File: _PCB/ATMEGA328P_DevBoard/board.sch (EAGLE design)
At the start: 35 parts, among them IC1 TP4056, IC2 DW01, J1 U-F-M5DD-Y-L, J2 TYPE-C-31-M-17, T1 FS8205A, U1 MT3608, U2 ATMEGA328P_TQFP

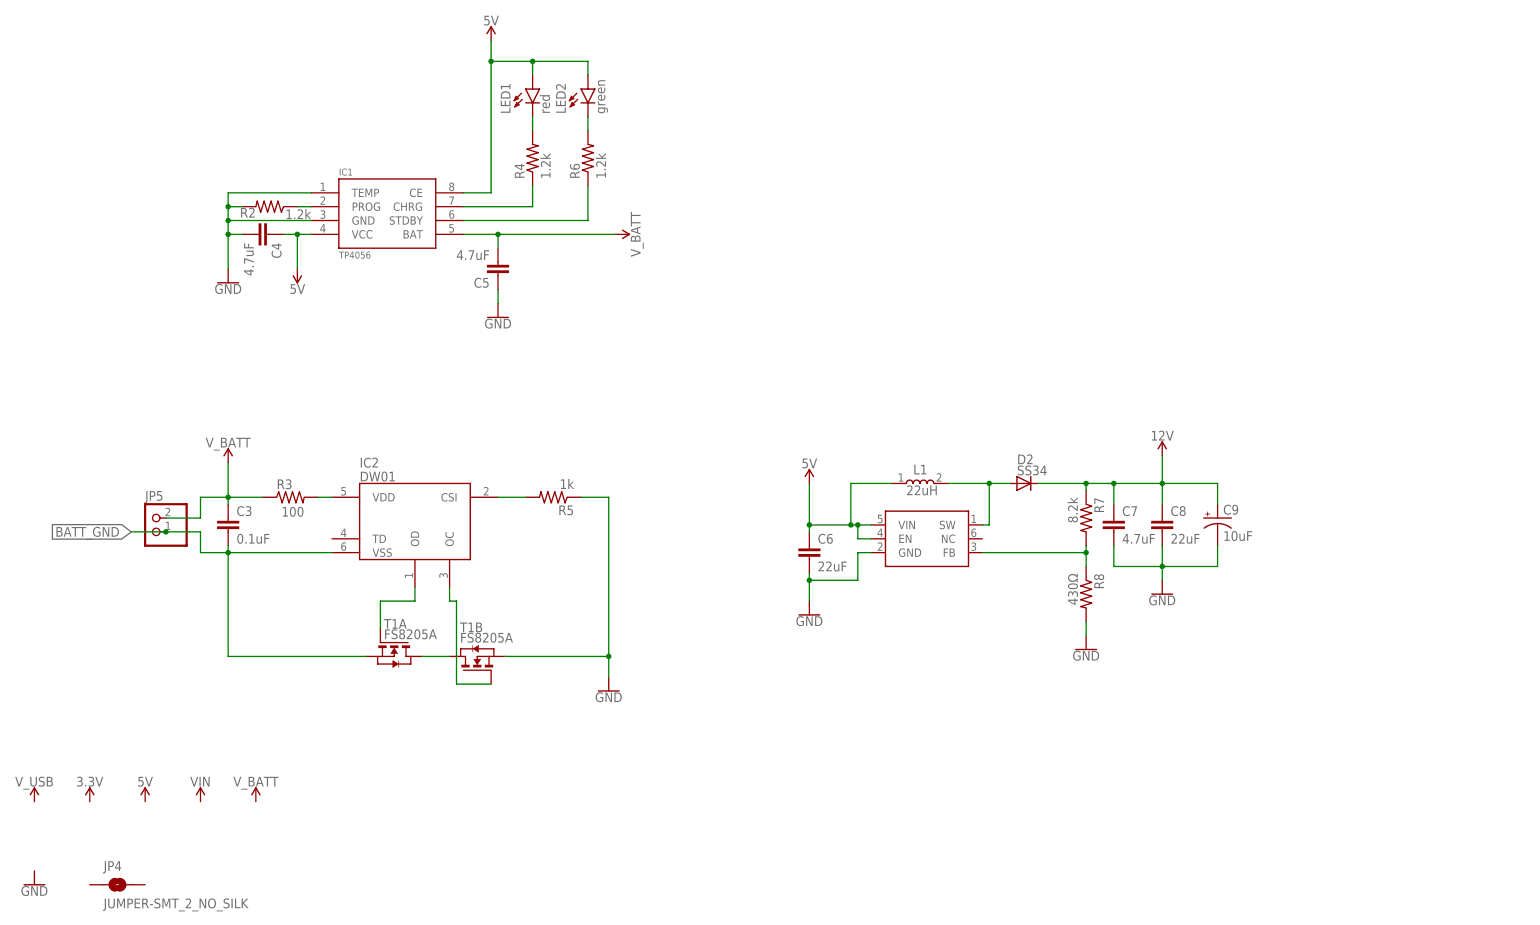
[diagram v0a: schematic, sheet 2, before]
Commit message: ESP12 PCB updated for JLCPCB
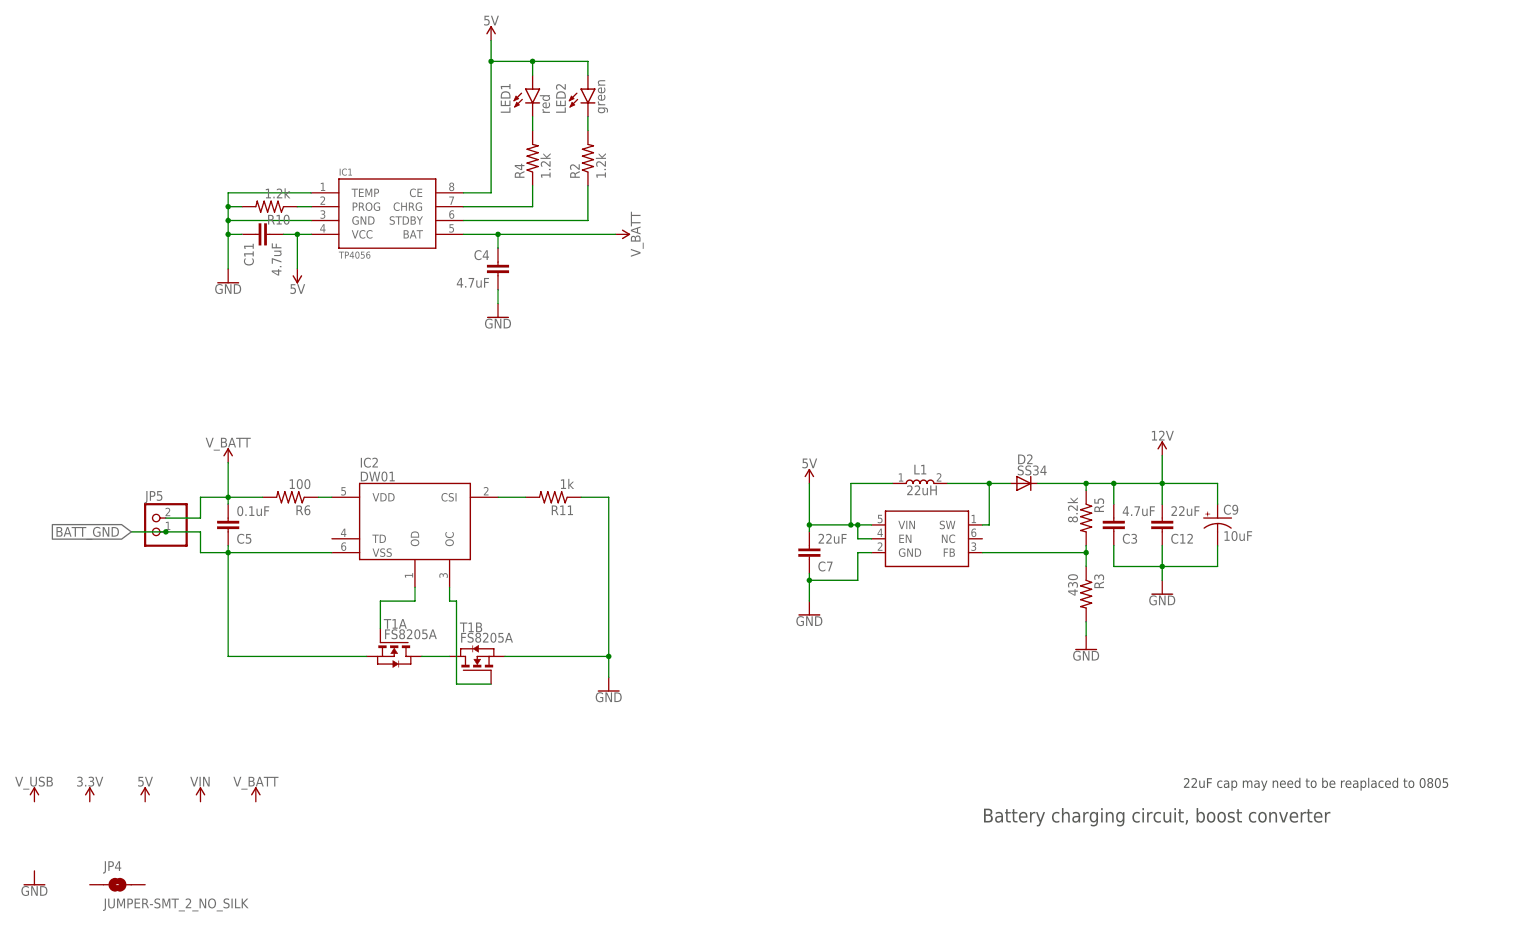
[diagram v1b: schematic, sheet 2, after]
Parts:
- removed C6, C8: 22uF, rcl:C-EUC0805
- removed R7: 8.2k, rcl:R-US_R0805
- removed R8: 430Ω, rcl:R-US_R0805
- added C10: 4.7n / 1kv, rcl:C-EUC0603
- added C11: 4.7uF, rcl:C-EUC0603
- added C12: 22uF, rcl:C-EUC0603
- added R10: 1.2k, rcl:R-US_R0603
- added R11: 1k, rcl:R-US_R0603
- added R9: 1M, rcl:R-US_R0603
- C3: value 0.1uF -> 4.7uF; device rcl:C-EUC0805 -> rcl:C-EUC0603
- C4: device rcl:C-EUC0805 -> rcl:C-EUC0603
- C5: value 4.7uF -> 0.1uF; device rcl:C-EUC0805 -> rcl:C-EUC0603
- C7: value 4.7uF -> 22uF; device rcl:C-EUC0805 -> rcl:C-EUC0603
- R2, R4: device rcl:R-US_R0805 -> rcl:R-US_R0603
- R3: value 100 -> 430; device rcl:R-US_R0805 -> rcl:R-US_R0603
- R5: value 1k -> 8.2k; device rcl:R-US_R0805 -> rcl:R-US_R0603
- R6: value 1.2k -> 100; device rcl:R-US_R0805 -> rcl:R-US_R0603
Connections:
- net 12V: now also C12.1, C3.1, R5.1; no longer C7.1, C8.1, R7.1
- net 5V: now also C11.1, C7.1; no longer C4.1, C6.1
- net BATT_GND: now also C5.2; no longer C3.2
- net GND: now also C11.2, C12.2, C3.2, C4.1, R10.2, R11.1, R3.2; no longer C4.2, C5.1, C6.2, C8.2, R2.2, R5.1, R8.2
- net N$14: now also R3.1, R5.2; no longer R7.2, R8.1
- net N$3: now also R2.1; no longer R6.1
- net N$4: now also R6.1; no longer R3.2
- net N$5: now also R11.2; no longer R5.2
- net N$8: now also R10.1; no longer R2.1
- net N$9: now also R2.2; no longer R6.2
- net V_BATT: now also C4.2, C5.1, R6.2; no longer C3.1, C5.2, R3.1
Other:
- note added: "22uF cap may need to be reaplaced to 0805"
- note added: "Battery charging circuit, boost converter"
- note added: "Power input"
- moved on the sheet: C3, C4, C5, C7, R2, R3, R5, R6
